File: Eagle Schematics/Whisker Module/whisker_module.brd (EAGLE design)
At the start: 45.4 x 80 mm, 30 parts, among them Q1 16MHZ, T1 BJT, T2 BJT, T3 BJT, T4 BJT

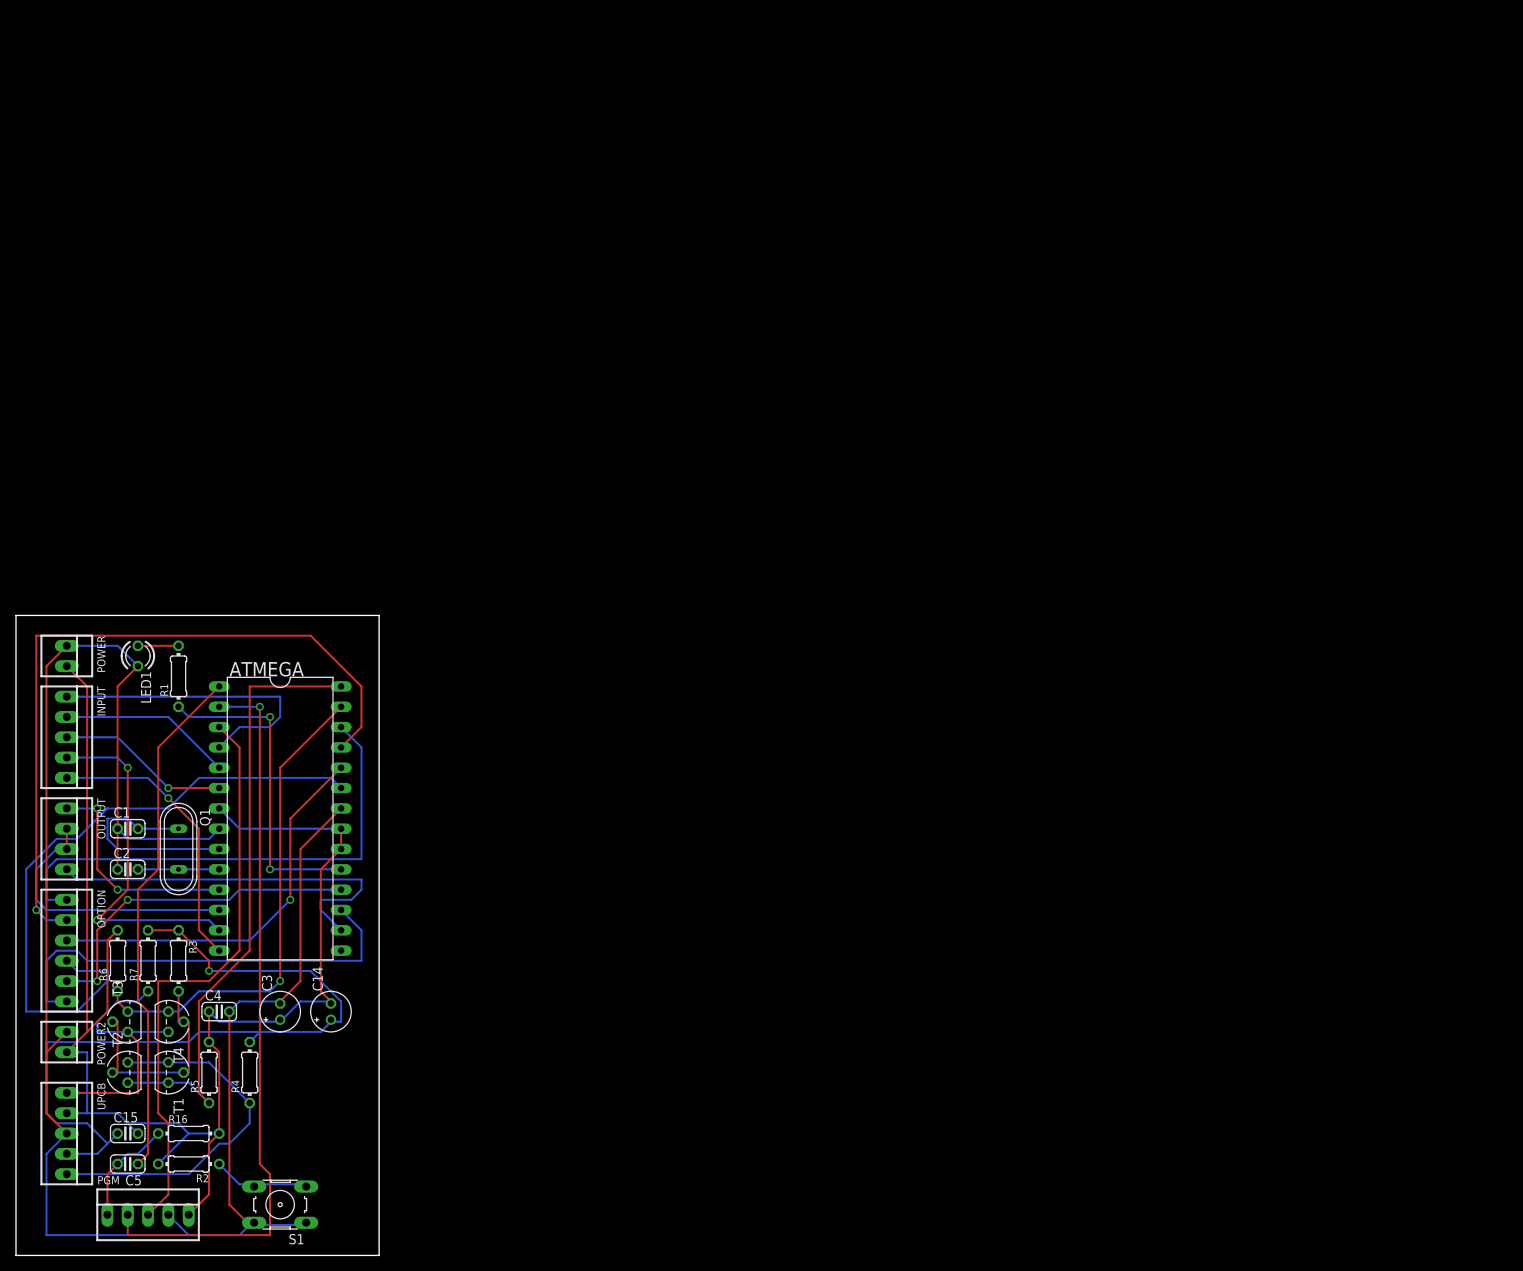
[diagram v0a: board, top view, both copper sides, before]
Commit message: Modified all schematics
Added a self debugging system.
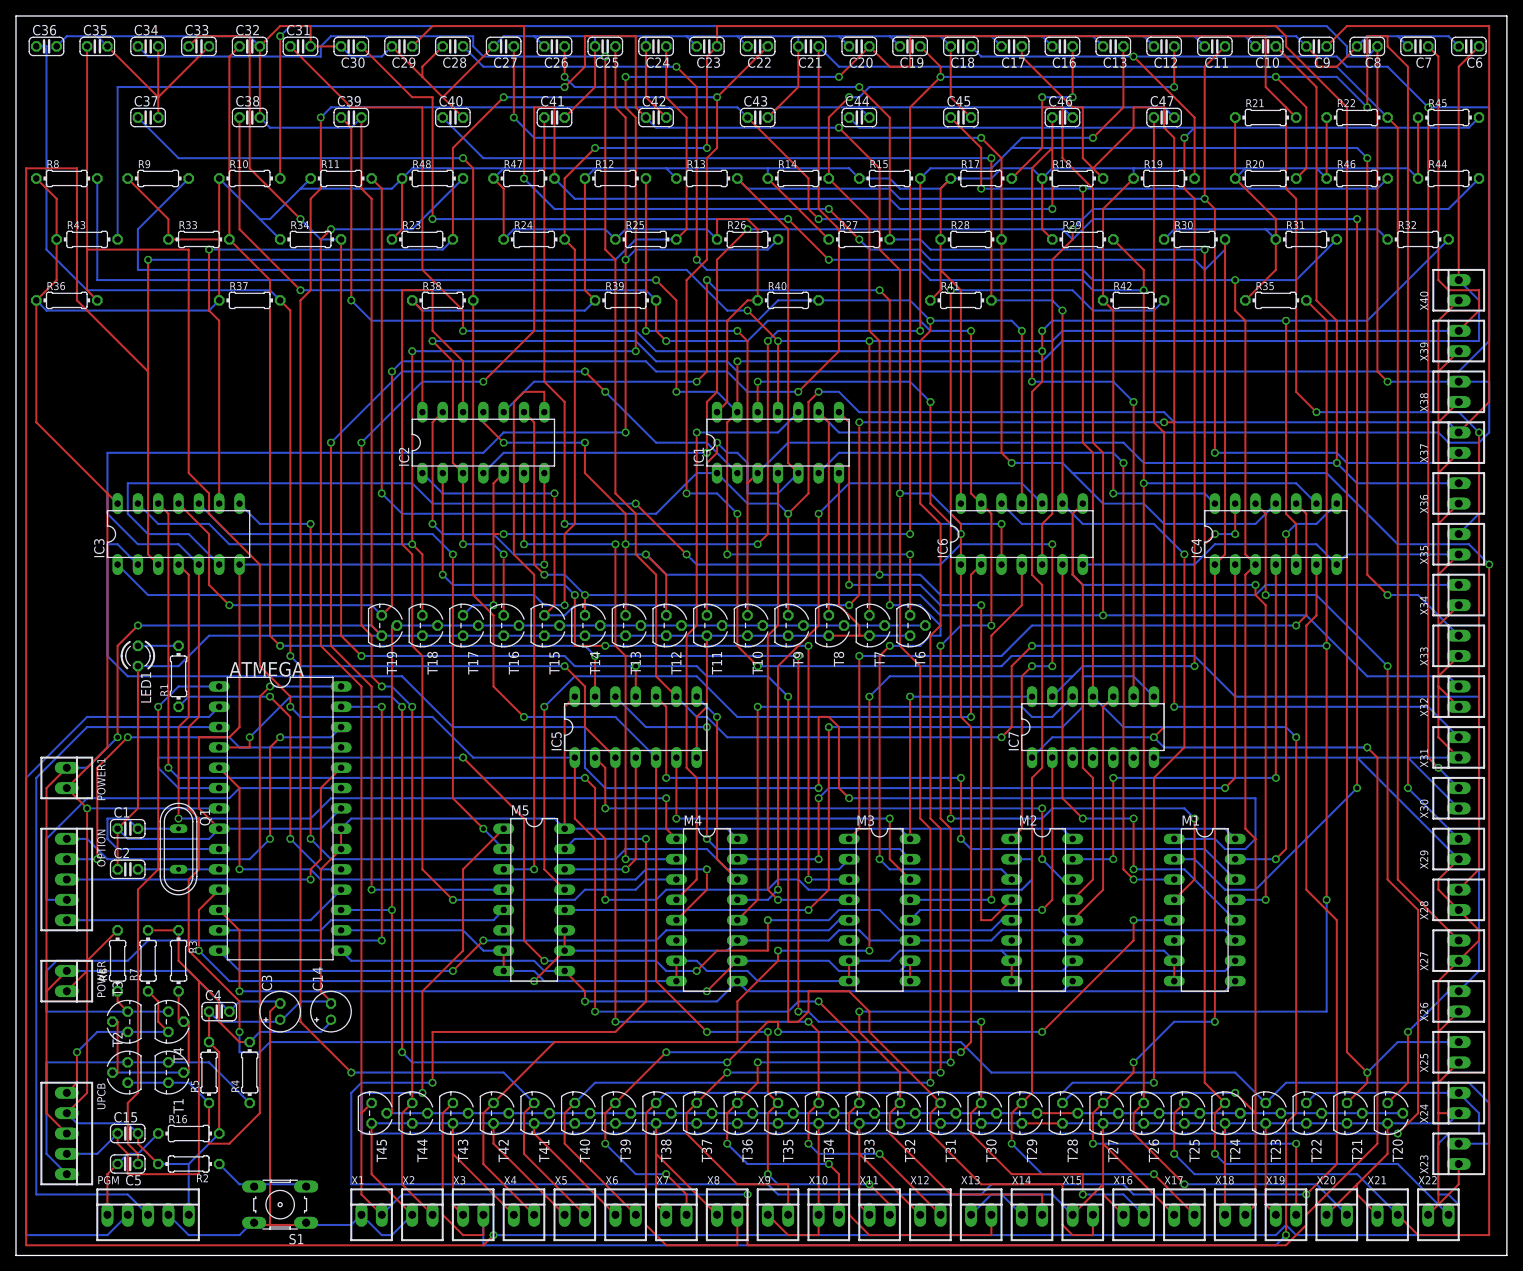
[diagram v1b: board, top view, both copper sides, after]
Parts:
- removed INPUT: 22-23-2051, con-molex:22-23-2051
- removed OUTPUT: 22-23-2041, con-molex:22-23-2041
- removed POWER2: 22-23-2021, con-molex:22-23-2021
- added C10, C11, C12, C13, C16, C17, C18, C19, C20, C21, C22, C23, C24, C25, C26, C27, C28, C29, C30, C31, C32, C33, C34, C35, C36, C37, C38, C39, C40, C41, C42, C43, C44, C45, C46, C47, C6, C7, C8, C9: 0.1uF, rcl:C025-024X044
- added IC1, IC2, IC3, IC4, IC5, IC6, IC7: 74LS14N, 74xx-us:DIL14
- added M1, M2, M3, M4, M5: CD74HCT151E, Custom:CD74HCT151E
- added POWER1, X1, X10, X11, X12, X13, X14, X15, X16, X17, X18, X19, X2, X20, X21, X22, X23, X24, X25, X26, X27, X28, X29, X3, X30, X31, X32, X33, X34, X35, X36, X37, X38, X39, X4, X40, X5, X6, X7, X8, X9: 22-23-2021, con-molex:22-23-2021
- added R10, R11, R12, R13, R14, R15, R17, R18, R19, R20, R21, R22, R23, R24, R25, R26, R27, R28, R29, R30, R31, R32, R33, R34, R35, R36, R37, R38, R39, R40, R41, R42, R43, R44, R45, R46, R47, R48, R8, R9: 10KOHM, rcl:0204/7
- added T10, T11, T12, T13, T14, T15, T16, T17, T18, T19, T20, T21, T22, T23, T24, T25, T26, T27, T28, T29, T30, T31, T32, T33, T34, T35, T36, T37, T38, T39, T40, T41, T42, T43, T44, T45, T6, T7, T8, T9: 2N3565, transistor:TO92
- OPTION: value (none) -> 22-23-2051; device con-molex:22-23-2061 -> con-molex:22-23-2051
- moved POWER 40.6 mm to (6.35, 34.3)
- moved OPTION 8.89 mm to (6.35, 47.0)
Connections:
- removed net IN1: ATMEGA.4, INPUT.1
- removed net IN2: ATMEGA.5, INPUT.2
- removed net IN3: ATMEGA.6, INPUT.3
- removed net IN4: ATMEGA.13, INPUT.4
- removed net IN5: ATMEGA.14, INPUT.5
- removed net OPTION6: ATMEGA.17, OPTION.6
- removed net OUT1: ATMEGA.11, OUTPUT.1
- removed net OUT2: ATMEGA.12, OUTPUT.2, OUTPUT.3
- removed net OUT3: ATMEGA.15
- removed net OUT4: ATMEGA.16, OUTPUT.4
- new net D1: IC1.12, M1.4
- new net D10: IC2.2, M3.3
- new net D11: IC2.4, M1.2
- new net D12: IC2.6, M4.2
- new net D13: IC3.12, M2.2
- new net D14: IC3.10, M5.2
- new net D15: IC3.8, M3.2
- new net D16: IC3.2, M1.1
- new net D17: IC3.4, M4.1
- new net D18: IC3.6, M2.1
- new net D19: IC4.12, M5.1
- new net D2: IC1.10, M4.4
- new net D20: IC4.10, M3.1
- new net D21: IC4.8, M1.15
- new net D22: IC4.2, M4.15
- new net D23: IC4.4, M2.15
- new net D24: IC4.6, M5.15
- new net D25: IC5.12, M3.15
- new net D26: IC5.10, M1.14
- new net D27: IC5.8, M4.14
- new net D28: IC5.2, M2.14
- new net D29: IC5.4, M5.14
- new net D3: IC1.8, M2.4
- new net D30: IC5.6, M3.14
- new net D31: IC6.12, M1.13
- new net D32: IC6.10, M4.13
- new net D33: IC6.8, M2.13
- new net D34: IC6.2, M5.13
- new net D35: IC6.4, M3.13
- new net D36: IC6.6, M1.12
- new net D37: IC7.12, M4.12
- new net D38: IC7.10, M2.12
- new net D39: IC7.8, M5.12
- new net D4: IC1.2, M5.4
- new net D40: IC7.2, M3.12
- new net D5: IC1.4, M3.4
- new net D6: IC1.6, M1.3
- new net D7: IC2.12, M4.3
- new net D8: IC2.10, M2.3
- new net D9: IC2.8, M5.3
- new net RESULT1: ATMEGA.4, M1.5
- new net RESULT2: ATMEGA.5, M4.5
- new net RESULT3: ATMEGA.6, M2.5
- new net RESULT4: ATMEGA.13, M5.5
- new net RESULT5: ATMEGA.14, M3.5
- new net SELECT1: ATMEGA.11, M1.11, M2.11, M3.11, M4.11, M5.10, M5.11
- new net SELECT2: ATMEGA.12, M1.10, M2.10, M3.10, M3.9, M4.10
- new net SELECT3: ATMEGA.15, M1.9, M2.9, M4.9, M5.9
- new net SELECT4: ATMEGA.16, M1.7, M1.8, M2.7, M2.8, M3.7, M3.8, M4.7, M4.8, M5.7, M5.8
- new net SELECT5: ATMEGA.17, T10.2, T11.2, T12.2, T13.2, T14.2, T15.2, T16.2, T17.2, T18.2, T19.2, T20.2, T21.2, T22.2, T23.2, T24.2, T25.2, T26.2, T27.2, T28.2, T29.2, T30.2, T31.2, T32.2, T33.2, T34.2, T35.2, T36.2, T37.2, T38.2, T39.2, T40.2, T41.2, T42.2, T43.2, T44.2, T45.2, T6.2, T7.2, T8.2, T9.2
- new net W1: C6.1, IC1.13, R8.2, T6.3, X40.2
- new net W10: C17.1, IC2.1, R18.2, T15.3, X31.2
- new net W11: C18.1, IC2.3, R19.2, T16.3, X30.2
- new net W12: C19.1, IC2.5, R20.2, T17.3, X29.2
- new net W13: C20.1, IC3.13, R21.2, T18.3, X28.2
- new net W14: C21.1, IC3.11, R22.2, T19.3, X27.2
- new net W15: C22.1, IC3.9, R23.2, T20.3, X26.2
- new net W16: C23.1, IC3.1, R24.2, T21.3, X25.2
- new net W17: C24.1, IC3.3, R25.2, T22.3, X24.2
- new net W18: C25.1, IC3.5, R26.2, T23.3, X23.2
- new net W19: C26.1, IC4.13, R27.2, T24.3, X22.2
- new net W2: C7.1, IC1.11, R9.2, T7.3, X39.2
- new net W20: C27.1, IC4.11, R28.2, T25.3, X21.2
- new net W21: C28.1, IC4.9, R29.2, T26.3, X20.2
- new net W22: C29.1, IC4.1, R30.2, T27.3, X19.2
- new net W23: C30.1, IC4.3, R31.2, T28.3, X18.2
- new net W24: C31.1, IC4.5, R32.2, T29.3, X17.2
- new net W25: C32.1, IC5.13, R33.2, T30.3, X16.2
- new net W26: C33.1, IC5.11, R34.2, T31.3, X15.2
- new net W27: C34.1, IC5.9, R35.2, T32.3, X14.2
- new net W28: C35.1, IC5.1, R36.2, T33.3, X13.2
- new net W29: C36.1, IC5.3, R37.2, T34.3, X12.2
- new net W3: C8.1, IC1.9, R10.2, T8.3, X38.2
- new net W30: C37.1, IC5.5, R38.2, T35.3, X11.2
- new net W31: C38.1, IC6.13, R39.2, T36.3, X10.2
- new net W32: C39.1, IC6.11, R40.2, T37.3, X9.2
- new net W33: C40.1, IC6.9, R41.2, T38.3, X8.2
- new net W34: C41.1, IC6.1, R42.2, T39.3, X7.2
- new net W35: C42.1, IC6.3, R43.2, T40.3, X6.2
- new net W36: C43.1, IC6.5, R44.2, T41.3, X5.2
- new net W37: C44.1, IC7.13, R45.2, T42.3, X4.2
- new net W38: C45.1, IC7.11, R46.2, T43.3, X3.2
- new net W39: C46.1, IC7.9, R47.2, T44.3, X2.2
- new net W4: C9.1, IC1.1, R11.2, T9.3, X37.2
- new net W40: C47.1, IC7.1, R48.2, T45.3, X1.2
- new net W5: C10.1, IC1.3, R12.2, T10.3, X36.2
- new net W6: C11.1, IC1.5, R13.2, T11.3, X35.2
- new net W7: C12.1, IC2.13, R14.2, T12.3, X34.2
- new net W8: C13.1, IC2.11, R15.2, T13.3, X33.2
- new net W9: C16.1, IC2.9, R17.2, T14.3, X32.2
- net 5V: now also IC1.14, IC2.14, IC3.14, IC4.14, IC5.14, IC6.14, IC7.14, M1.16, M2.16, M3.16, M4.16, M5.16, POWER1.2, R10.1, R11.1, R12.1, R13.1, R14.1, R15.1, R17.1, R18.1, R19.1, R20.1, R21.1, R22.1, R23.1, R24.1, R25.1, R26.1, R27.1, R28.1, R29.1, R30.1, R31.1, R32.1, R33.1, R34.1, R35.1, R36.1, R37.1, R38.1, R39.1, R40.1, R41.1, R42.1, R43.1, R44.1, R45.1, R46.1, R47.1, R48.1, R8.1, R9.1; no longer POWER2.2
- net GND: now also C10.2, C11.2, C12.2, C13.2, C16.2, C17.2, C18.2, C19.2, C20.2, C21.2, C22.2, C23.2, C24.2, C25.2, C26.2, C27.2, C28.2, C29.2, C30.2, C31.2, C32.2, C33.2, C34.2, C35.2, C36.2, C37.2, C38.2, C39.2, C40.2, C41.2, C42.2, C43.2, C44.2, C45.2, C46.2, C47.2, C6.2, C7.2, C8.2, C9.2, IC1.7, IC2.7, IC3.7, IC4.7, IC5.7, IC6.7, IC7.7, POWER1.1, T10.1, T11.1, T12.1, T13.1, T14.1, T15.1, T16.1, T17.1, T18.1, T19.1, T20.1, T21.1, T22.1, T23.1, T24.1, T25.1, T26.1, T27.1, T28.1, T29.1, T30.1, T31.1, T32.1, T33.1, T34.1, T35.1, T36.1, T37.1, T38.1, T39.1, T40.1, T41.1, T42.1, T43.1, T44.1, T45.1, T6.1, T7.1, T8.1, T9.1, X1.1, X10.1, X11.1, X12.1, X13.1, X14.1, X15.1, X16.1, X17.1, X18.1, X19.1, X2.1, X20.1, X21.1, X22.1, X23.1, X24.1, X25.1, X26.1, X27.1, X28.1, X29.1, X3.1, X30.1, X31.1, X32.1, X33.1, X34.1, X35.1, X36.1, X37.1, X38.1, X39.1, X4.1, X40.1, X5.1, X6.1, X7.1, X8.1, X9.1; no longer POWER2.1
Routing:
- net GND: track 230.3 -> 1549.1 mm, vias 0 -> 3
- net 5V: track 186.6 -> 966.0 mm, vias 0 -> 3
- net W17: track 0.00 -> 526.7 mm, vias 0 -> 2
- net W40: track 0.00 -> 457.7 mm, vias 0 -> 4
- net W27: track 0.00 -> 429.8 mm, vias 0 -> 6
- net W18: track 0.00 -> 392.4 mm, vias 0 -> 3
- net W11: track 0.00 -> 377.6 mm, vias 0 -> 6
- net W16: track 0.00 -> 370.8 mm, vias 0 -> 4
- net W36: track 0.00 -> 365.9 mm, vias 0 -> 4
- net W13: track 0.00 -> 350.1 mm, vias 0 -> 7
- net W15: track 0.00 -> 347.0 mm, vias 0 -> 7
- net W14: track 0.00 -> 346.5 mm, vias 0 -> 3
- net W38: track 0.00 -> 343.9 mm, vias 0 -> 4
- net W24: track 0.00 -> 340.5 mm, vias 0 -> 6
- net W20: track 0.00 -> 338.9 mm, vias 0 -> 5
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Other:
- board size 45.4 x 80 mm -> 186.4 x 154.9 mm
